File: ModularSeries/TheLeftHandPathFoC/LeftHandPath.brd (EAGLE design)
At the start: 73 x 48 mm, 63 parts, among them Q1 2N3906, Q2 2N3904, Q3 2N3904, Q4 2N3906

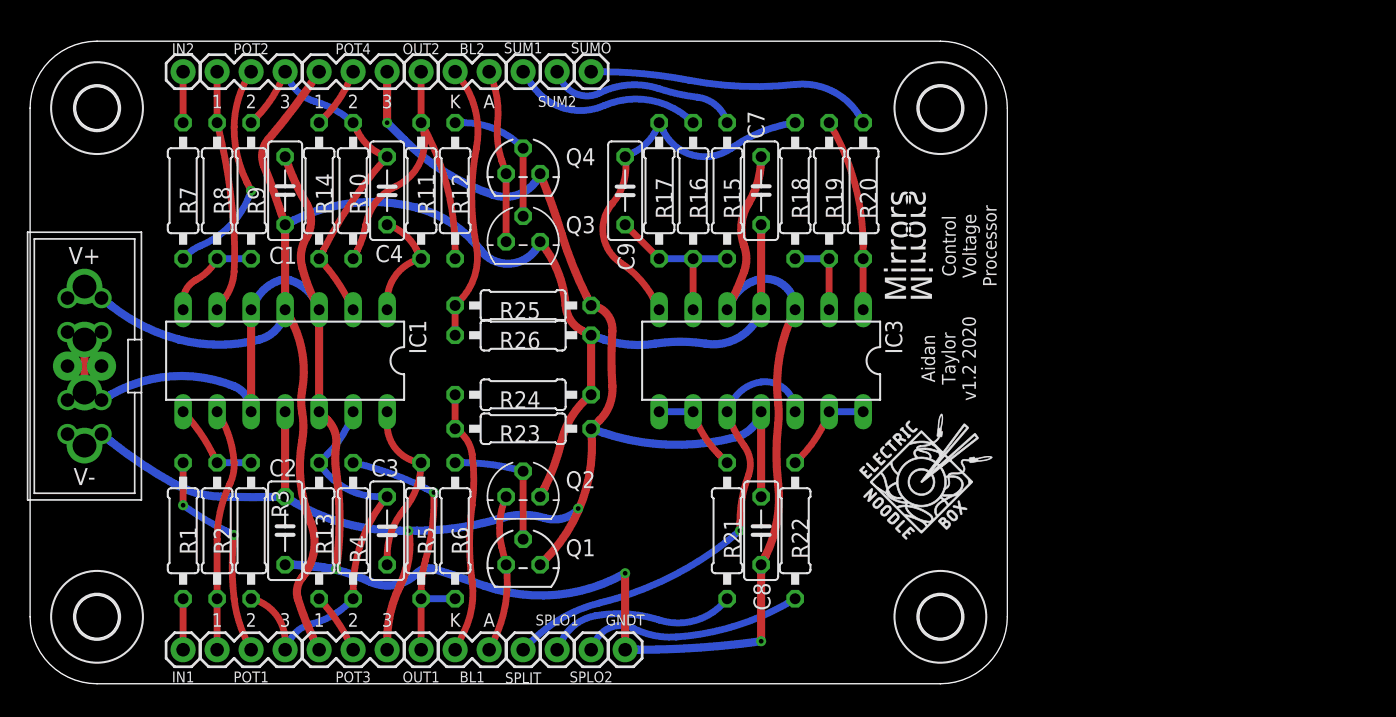
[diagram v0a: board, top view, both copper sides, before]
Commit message: Portals BOM update, Ffrydiau project added
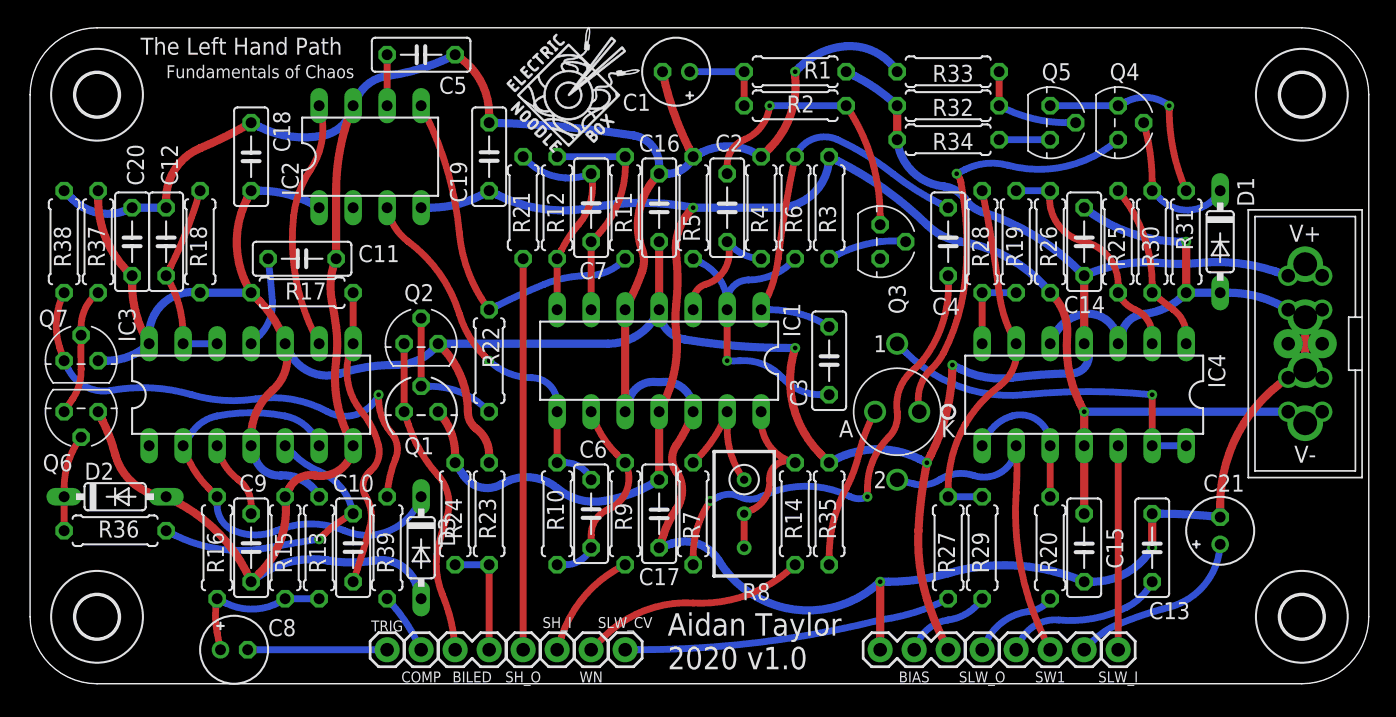
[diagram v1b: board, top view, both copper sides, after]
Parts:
- removed BL2: 2XWIREPAD, ElectricNoodleBox:1X02
- removed IN1, IN2, OUT2, SUM1, SUM2, SUMO: 1XWIREPAD, ElectricNoodleBox:1X01
- removed POT1, POT2, POT3, POT4: B100K, ElectricNoodleBox:1X03
- removed U$2: (no value), ElectricNoodleBox:LOGO10X10
- added BIAS, SW1: 3XWIREPAD, ElectricNoodleBox:1X03
- added C10: 2.2nF, rcl:C050-025X075
- added C11: 10nF, rcl:C050-025X075
- added C12, C14, C15, C16, C17, C18, C19, C20: 100nF, rcl:C050-025X075
- added C13, C6: 22pF, rcl:C050-025X075
- added C21: BP 4.7µF, rcl:E2-5
- added C5: 47nF, rcl:C050-025X075
- added D1, D2, D3: BAT85, ElectricNoodleBox:DO35-7
- added IC2: (no value), ElectricNoodleBox:DIL08
- added IC4: (no value), ElectricNoodleBox:DIL14
- added OC1: OPTOCOUPLERSILONEX, ElectricNoodleBox:SILONEX_OPTOCOUPLER
- added Q5: 2N7000, ElectricNoodleBox:TO92
- added Q6, Q7: 2N3904, transistor:TO92
- added R27, R28, R29: 100K, rcl:0207/7
- added R30, R31: 10K, rcl:0207/7
- added R32: 47K, rcl:0207/7
- added R33, R36, R37: 15K, rcl:0207/7
- added R34, R35: 4K7, rcl:0207/7
- added R38: 470Ω, rcl:0207/7
- added R39: 220Ω, rcl:0207/7
- added SLW_I, SLW_O, TRIG: 1XWIREPAD, ElectricNoodleBox:1X01
- C1: value 100nF -> 1µF; device rcl:C050-025X075 -> rcl:E2-5
- C3: value 22pF -> 10pF
- C4: value 22pF -> 100nF
- C7: value 100nF -> 15pF
- C8: value 100nF -> 4.7µF; device rcl:C050-025X075 -> rcl:E2-5
- C9: value 22pF -> 10nF
- IC3: value (none) -> 556_DUALTIMERDIL14
- Q4: value 2N3906 -> 2N7000; device transistor-pnp:TO92 -> ElectricNoodleBox:TO92
- R1, R2: value 100K -> 470K; device rcl:0207/10 -> rcl:0207/7
- R10, R16, R19, R3, R9: value 100K -> 10K; device rcl:0207/10 -> rcl:0207/7
- R11, R13, R15, R20, R21, R23, R24: device rcl:0207/10 -> rcl:0207/7
- R12: value 10K -> 1K; device rcl:0207/10 -> rcl:0207/7
- R14: value 100K -> 100Ω; device rcl:0207/10 -> rcl:0207/7
- R17: value 100K -> 20K; device rcl:0207/10 -> rcl:0207/7
- R18, R7: value 100K -> 1K; device rcl:0207/10 -> rcl:0207/7
- R22: value 100Ω -> 10K; device rcl:0207/10 -> rcl:0207/7
- R25: value 4K7 -> 10K; device rcl:0207/10 -> rcl:0207/7
- R26: value 4K7 -> 47K; device rcl:0207/10 -> rcl:0207/7
- R4: value 100K -> 2M; device rcl:0207/10 -> rcl:0207/7
- R5: value 1K -> 10K; device rcl:0207/10 -> rcl:0207/7
- R6: value 10K -> 470K; device rcl:0207/10 -> rcl:0207/7
- R8: device rcl:0207/10 -> rcl:RTRIM3296W
- moved WP1 91.2 mm to (95.2, 25.4)
- moved H3 90.0 mm to (95.0, 44.0)
- moved H4 90.0 mm to (95.0, 5.00)
- moved H2 63.0 mm to (5.00, 44.0)
- moved H1 63.0 mm to (5.00, 5.00)
- moved R1 57.1 mm to (57.1, 45.7), turned to 0 degrees
- moved R2 53.6 mm to (57.1, 43.2), turned to 180 degrees
- moved R3 49.5 mm to (59.7, 35.6), turned to 90 degrees
- moved R8 46.2 mm to (53.3, 12.7), turned to 180 degrees
- moved R7 45.1 mm to (49.5, 12.7), turned to 90 degrees
- moved R25 44.7 mm to (81.3, 33.0), turned to 90 degrees
- moved Q4 44.6 mm to (81.3, 41.9), turned to 270 degrees
- moved R18 44.6 mm to (12.7, 33.0), turned to 90 degrees
- moved R16 44.5 mm to (14.0, 10.2), turned to 90 degrees
- moved R14 43.0 mm to (57.1, 12.7)
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- renumbered BL1 to BILED, GNDT to SLW_CV, OUT1 to COMP, SPLIT to SH_O, SPLO1 to SH_I, SPLO2 to WN
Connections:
- new net N$35: BILED.2, Q1.3, Q2.3
- new net N$36: BILED.1, R23.1, R24.2
- new net N$37: IC4.2, R19.2, R25.1, R26.2
- new net N$38: IC4.6, R27.2, R28.1, R29.2
- new net N$39: IC4.1, R25.2, R30.1
- new net N$40: D1.C, Q4.2, R30.2
- new net N$41: Q4.1, Q5.1, R31.2
- new net N$42: C21.+, SW1.3
- new net N$43: Q5.2, R32.1, R33.2
- new net N$44: Q5.3, R34.1
- new net N$45: OC1.A, R35.1
- new net N$46: C13.2, SW1.1
- new net N$47: R27.1, SLW_CV.1
- new net N$48: BIAS.2, R29.1
- new net N$49: Q6.1, Q7.2, R37.1
- new net N$50: Q7.3, R38.2, R39.1
- new net N$51: COMP.1, R39.2
- new net N$52: D2.C, Q6.2, R36.1
- new net OPTO_KATHODE: OC1.K, Q4.3
- net +12V: now also BIAS.3, C14.2, C16.2, C18.2, C20.2, IC2.1, IC3.10, IC3.14, IC4.4, Q7.1, R1.2, R13.1, R17.1, R18.1, R23.2, R32.2, R34.2, R35.2, R37.2; no longer C1.1, C7.1, POT3.1, POT4.1, Q3.1, R24.1, R26.1
- net -12V: now also C15.1, C17.1, C19.1, IC2.4, IC4.11, R24.1, R26.1, R3.2; no longer C2.2, C8.2, IC3.11, POT3.3, POT4.3, Q4.1, R23.2, R25.2
- net AGND: now also BIAS.1, C1.-, C11.1, C12.1, C13.1, C14.1, C15.2, C16.1, C17.2, C18.1, C19.2, C20.1, C21.-, C5.1, C9.1, D1.A, D2.A, D3.A, IC2.7, IC3.7, IC4.3, IC4.5, Q6.3, R15.2, R31.1, R33.1, R38.1, R4.2, R5.2; no longer C1.2, C2.1, C7.2, C8.1, IC1.3, IC3.3, IC3.5, SLW_CV.1
- net N$1: now also C1.+, R1.1, R2.2; no longer POT1.2, R1.2
- net N$10: now also C6.1, IC1.9, R10.1, R9.2; no longer IC3.2, R18.2, R19.1
- net N$11: now also C6.2, IC1.8, IC2.3, R10.2; no longer IC1.6, POT2.1, R8.1
- net N$12: now also C5.2, IC2.6; no longer IC1.7, R8.2, R9.1
- net N$13: now also IC2.5, R11.1, R22.1; no longer C4.1, IC1.2, POT2.3, R10.1, R14.2, R9.2
- net N$14: now also C7.1, IC1.6; no longer OUT2.1, R10.2
- net N$15: now also C7.2, IC1.7, R12.2, R21.1; no longer C4.2, IC1.1, R11.1
- net N$16: now also R9.1, SH_I.1; no longer IN2.1, R7.1
- net N$17: now also C10.2, IC3.5, R36.2; no longer Q3.2, Q4.2, R12.2
- net N$18: now also C8.+, R13.2, R15.1, R16.1; no longer BL2.1, Q3.3, Q4.3
- net N$19: now also D3.C, IC3.2, IC3.6, R16.2; no longer BILED.1, Q1.3, Q2.3
- net N$2: now also C2.1, Q3.3; no longer IC1.9, POT1.1
- net N$20: now also R14.2, WN.1; no longer POT3.2, R13.1
- net N$21: now also IC3.3; no longer IC3.6, R15.2, R16.2, R17.1
- net N$22: now also C10.1, IC3.8, R17.2; no longer POT4.2, R14.1
- net N$23: now also C11.2, IC3.11; no longer C9.1, IC3.7, R17.2, R18.1
- net N$24: now also C12.2, IC3.12, IC3.13, R18.2; no longer IC3.1, R19.2, R20.1
- net N$25: now also IC2.8, IC3.9; no longer R20.2, SUMO.1
- net N$26: now also C8.-, TRIG.1; no longer R16.1, SUM1.1
- net N$27: now also IC4.12, SLW_I.1; no longer R15.1, SUM2.1
- net N$28: now also IC4.13, IC4.14, OC1.1; no longer IC3.8, IC3.9, R21.1
- net N$29: now also IC4.7, R19.1, R28.2; no longer IC3.13, IC3.14, R22.1
- net N$3: now also Q3.2, R3.1; no longer POT2.2, R7.2
- net N$30: now also IC4.9, OC1.2, SW1.2; no longer IC3.10, IC3.12, SH_O.1
- net N$31: now also IC4.10, IC4.8, R20.1; no longer R21.2, SH_I.1
- net N$32: now also R20.2, SLW_O.1; no longer R22.2, WN.1
- net N$33: now also R21.2, SH_O.1; no longer BILED.2, R23.1, R24.2
- net N$34: now also Q1.2, Q2.2, R22.2; no longer BL2.2, R25.1, R26.2
- net N$4: now also C2.2, IC1.3, R4.1; no longer IC1.8, R2.2, R3.1
- net N$5: now also IC1.2, R5.1, R6.1; no longer IC1.13, POT1.3, R13.2, R3.2, R4.1
- net N$6: now also C3.2, C4.1, IC1.1, R6.2; no longer COMP.1, R4.2, R5.2, R6.1
- net N$7: now also C4.2, R7.1; no longer C3.2, IC1.14, R5.1
- net N$8: now also IC1.13, R7.2, R8.1; no longer Q1.2, Q2.2, R6.2
- net N$9: now also IC1.14, R14.1, R8.2, R8.3; no longer IN1.1, R1.1
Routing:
- net AGND: track 166.3 -> 308.8 mm, vias 3 -> 4
- net +12V: track 125.1 -> 211.5 mm, vias 0 -> 3
- net N$50: track 0.00 -> 37.6 mm, vias 0 -> 1
- net OPTO_KATHODE: track 0.00 -> 31.0 mm, vias 0 -> 1
- net N$38: track 0.00 -> 27.1 mm
- net N$47: track 0.00 -> 24.5 mm
- net N$35: track 0.00 -> 23.8 mm
- net N$19: track 11.6 -> 34.0 mm
- net N$7: track 12.8 -> 34.5 mm, vias 0 -> 2
- net N$23: track 27.4 -> 6.80 mm
- net N$28: track 7.14 -> 26.2 mm, vias 0 -> 1
- net N$22: track 4.59 -> 22.3 mm
- net N$37: track 0.00 -> 16.5 mm
- net N$41: track 0.00 -> 15.5 mm, vias 0 -> 1
- net N$42: track 0.00 -> 13.3 mm
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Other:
- board size 73 x 48 mm -> 100 x 49 mm
- board text added: "Aidan Taylor 2020 v1.0"
- board text added: "Fundamentals of Chaos"
- board text added: "The Left Hand Path"
- board text removed: "1"
- board text removed: "2"
- board text removed: "3"
- board text removed: "A"
- board text removed: "Aidan Taylor v1.2 2020"
- board text removed: "Control Voltage Processor"
- board text removed: "K"
- board text removed: "Mirrors"

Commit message: Panel wiring diagram for TLHP added
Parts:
- C7: value 15pF -> 10nF
- R11: value 1K -> 10K
- R12: value 1K -> DNF
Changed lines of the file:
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@@
 <attribute name="VALUE" x="44.704" y="9.271" size="1.27" layer="27" ratio="10" rot="R90"/>
 </element>
-<element name="C7" library="rcl" library_urn="urn:adsk.eagle:library:334" package="C050-025X075" package3d_urn="urn:adsk.eagle:package:23637/1" value="15pF" x="41.91" y="35.56" smashed="yes" rot="R90">
+<element name="C7" library="rcl" library_urn="urn:adsk.eagle:library:334" package="C050-025X075" package3d_urn="urn:adsk.eagle:package:23637/1" value="10nF" x="41.91" y="35.56" smashed="yes" rot="R90">
 <attribute name="NAME" x="41.021" y="30.226" size="1.27" layer="25" ratio="10"/>
 <attribute name="POPULARITY" value="29" x="78.74" y="52.07" size="1.778" layer="27" rot="R90" display="off"/>
@@
 <attribute name="VALUE" x="39.9288" y="10.414" size="1.27" layer="27" ratio="10" rot="R90"/>
 </element>
-<element name="R11" library="rcl" library_urn="urn:adsk.eagle:library:334" package="0207/7" package3d_urn="urn:adsk.eagle:package:23493/2" value="1K" x="44.45" y="35.56" smashed="yes" rot="R90">
+<element name="R11" library="rcl" library_urn="urn:adsk.eagle:library:334" package="0207/7" package3d_urn="urn:adsk.eagle:package:23493/2" value="10K" x="44.45" y="35.56" smashed="yes" rot="R90">
 <attribute name="NAME" x="44.958" y="33.655" size="1.27" layer="25" ratio="10" rot="R90"/>
 <attribute name="POPULARITY" value="46" x="105.41" y="104.14" size="1.778" layer="27" rot="R90" display="off"/>
@@
 <attribute name="VALUE" x="45.0088" y="33.274" size="1.27" layer="27" ratio="10" rot="R90"/>
 </element>
-<element name="R12" library="rcl" library_urn="urn:adsk.eagle:library:334" package="0207/7" package3d_urn="urn:adsk.eagle:package:23493/2" value="1K" x="39.37" y="35.56" smashed="yes" rot="R270">
+<element name="R12" library="rcl" library_urn="urn:adsk.eagle:library:334" package="0207/7" package3d_urn="urn:adsk.eagle:package:23493/2" value="DNF" x="39.37" y="35.56" smashed="yes" rot="R270">
 <attribute name="NAME" x="39.878" y="33.655" size="1.27" layer="25" ratio="10" rot="R90"/>
 <attribute name="POPULARITY" value="46" x="-21.59" y="-43.18" size="1.778" layer="27" rot="R270" display="off"/>

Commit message: Fields added and various updates to designs
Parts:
- removed R3: 10K, rcl:0207/7
- R14: value 100Ω -> 1K
- R19: value 10K -> 100K
- R26: value 47K -> 75K
- R31: value 10K -> 100Ω
- R33: value 15K -> 1K5
- R7: value 1K -> 10K
- R8: value 100K -> 470K
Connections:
- removed net N$3: Q3.2, R3.1
- removed net N$31 (its old number): IC4.10, IC4.8, R20.1
- new net N$46: IC4.8, IC4.9, R20.1
- net -12V: no longer R3.2
- net AGND: now also Q3.2
- net N$30: now also IC4.10; no longer IC4.9
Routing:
- net N$31: track 11.8 -> 0.00 mm
- net N$31 (its old number): track 10.6 -> 0.00 mm
- net N$30: track 25.2 -> 17.8 mm
- net -12V: track 128.1 -> 122.0 mm
- net N$3: track 5.93 -> 0.00 mm
- net AGND: track 308.8 -> 314.0 mm
